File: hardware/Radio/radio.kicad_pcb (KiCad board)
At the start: 4 copper layers, 40.9 x 24.9 mm, 92 parts, among them J1 edgeMountSMA, J2 edgeMountSMA, P1 CONN_11X2, P2 CONN_1, P3 CONN_8, P4 CONN_5X2, P5 CONN_1, P6 CONN_1, U1 AX503, U2 PE42424, U3 RF5110G, U4 MKL26Z128VLH4, U6 MICRO-B_USB, X1 TCXO

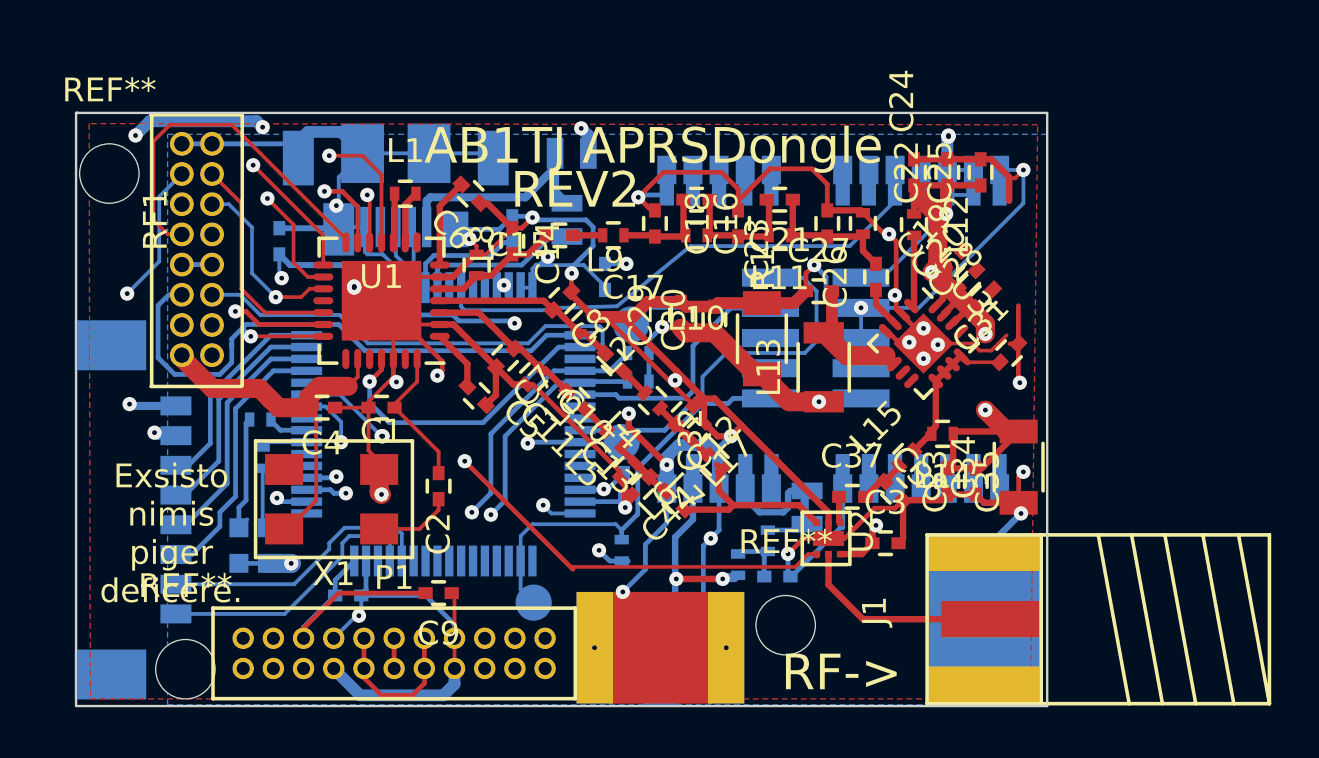
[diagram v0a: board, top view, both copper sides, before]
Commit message: Annotated the schematic and board
Made the numbers increase by 100, so I can just copy this in.
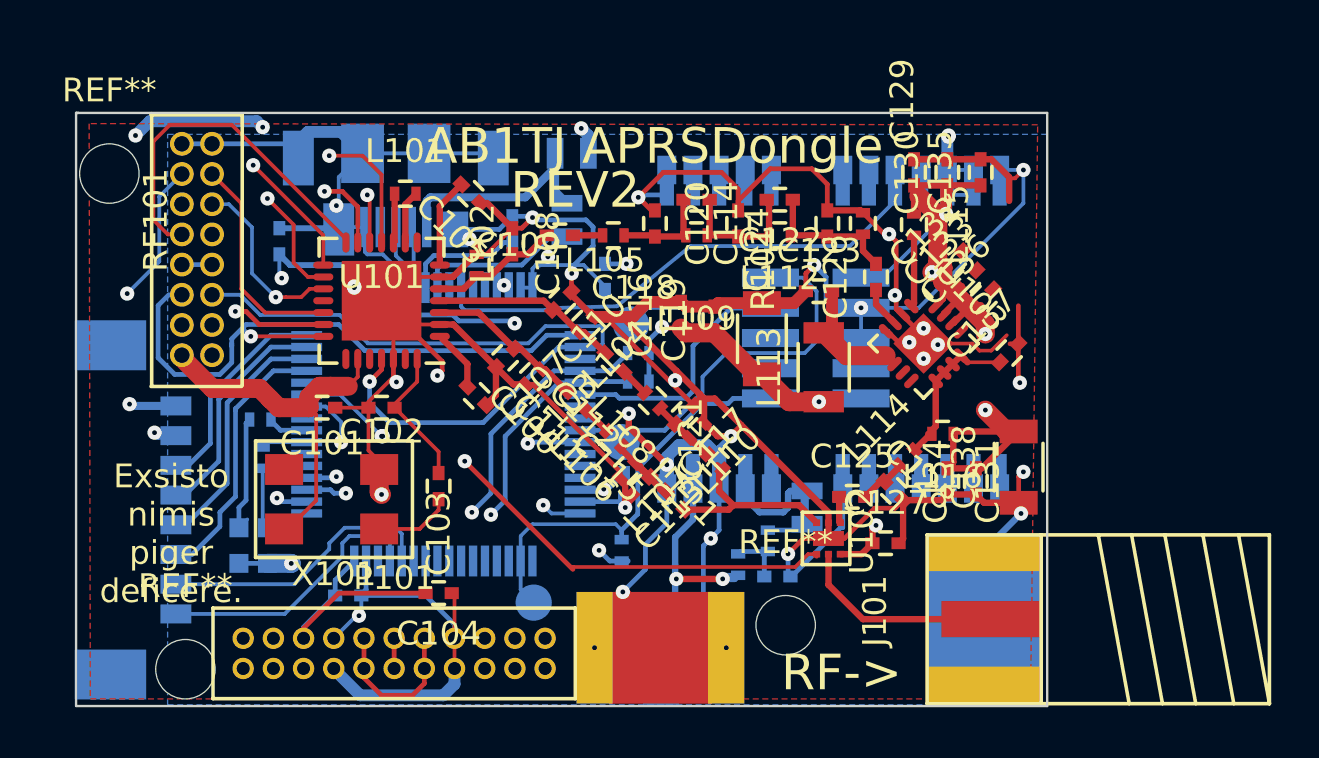
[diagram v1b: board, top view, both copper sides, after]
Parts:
- removed JMP2: SJMPClosed, SMDJMP-CLOSED
- removed RF2: NEO7, NEO-7
- added JMP103: SJMPClosed, hardwareRev1:SMDJMP-CLOSED, B.Cu at (93.9, 68.7)
- added RF102: NEO7, hardwareRev1:NEO-7, B.Cu at (87.0, 54.5)
- C102: renamed from C1; value C -> 6.8pf
- C103: renamed from C2; value C -> 10pf
- C105: renamed from C6; value C -> 100nf
- C106: renamed from C5; value C -> 100nf
- C134: renamed from C33; value C -> DNP
- C139: renamed from C39; value C -> 1uf
- C140: renamed from C40; value C -> 1uf
- C142: renamed from C42; value C -> 1uf
- C143: renamed from C41; value C -> 1uf
- L101: renamed from L1; value 60nh -> 22nh
- L110: renamed from L17; value INDUCTOR -> DNP
- R102: renamed from R4; value R -> 80
- R103: renamed from R5; value R -> 80
- renumbered C4 to C101, C9 to C104, C7 to C107, C14 to C108, C15 to C109, C8 to C110, C11 to C111, C10 to C112, C44 to C113, C16 to C114, C13 to C115, C29 to C116, C12 to C117, C17 to C118, C30 to C119, C18 to C120, C32 to C121, C21 to C122, C27 to C123, C23 to C124, C37 to C125, C26 to C126, C3 to C127, C36 to C128, C24 to C129, C22 to C130, C35 to C131, C19 to C132, C20 to C133, C25 to C135, C28 to C136, C31 to C137, C34 to C138, C38 to C141, C43 to C144, D1 to D101, D2 to D102, J1 to J101, J2 to J102, JMP4 to JMP101, JMP3 to JMP102, L8 to L102, L3 to L103, L2 to L104, L9 to L105, L5 to L106, L6 to L107, L4 to L108, L10 to L109, L7 to L111, L11 to L112, L13 to L113, L15 to L114, L12 to L115, L14 to L116, L16 to L117, P1 to P101, P3 to P102, P6 to P103, P2 to P104, P5 to P105, P4 to P106, R1 to R101, R6 to R104, R3 to R105, R2 to R106, R7 to R107, RF1 to RF101, U1 to U101, U2 to U102, U3 to U103, U6 to U104, U4 to U105, X1 to X101
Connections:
- D101 pad 1: Net-(D1-Pad1) -> (no net)
- D102 pad 1: Net-(D2-Pad1) -> (no net)
- R102 pad 1: Net-(D1-Pad1) -> (no net)
- R103 pad 1: Net-(D2-Pad1) -> (no net)
- RF101 pad 5: /DATA -> /Data
- U101 pad 11: /DATA -> (no net)
- U105 pad 10: /GPSTX -> (no net)
- U105 pad 59: /DATA -> /Data
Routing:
- net /Data: track 0.00 -> 29.0 mm, vias 0 -> 3
- net /DATA: track 29.0 -> 0.00 mm, vias 3 -> 0
- net (no net): track 0.00 -> 7.82 mm
- net Net-(D1-Pad1): track 5.23 -> 0.00 mm
- net Net-(JMP2-Pad1): track 4.97 -> 0.00 mm
- net Net-(JMP103-Pad1): track 0.00 -> 4.97 mm
- net Net-(D2-Pad1): track 2.58 -> 0.00 mm
- net Net-(RF2-Pad21): track 1.05 -> 0.00 mm
- net Net-(RF2-Pad19): track 1.05 -> 0.00 mm
- net Net-(RF2-Pad18): track 1.05 -> 0.00 mm
- net Net-(RF2-Pad14): track 1.05 -> 0.00 mm
- net Net-(RF102-Pad21): track 0.00 -> 1.05 mm
- net Net-(RF102-Pad19): track 0.00 -> 1.05 mm
- net Net-(RF102-Pad18): track 0.00 -> 1.05 mm
- net Net-(RF102-Pad14): track 0.00 -> 1.05 mm
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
